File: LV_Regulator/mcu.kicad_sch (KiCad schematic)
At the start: 58 parts, among them J5 SWD, J6 2169890001, U10 25CSM04xxSN, U4 STM32F103C8Tx, Y1 32.768kHz, Y2 8MHz

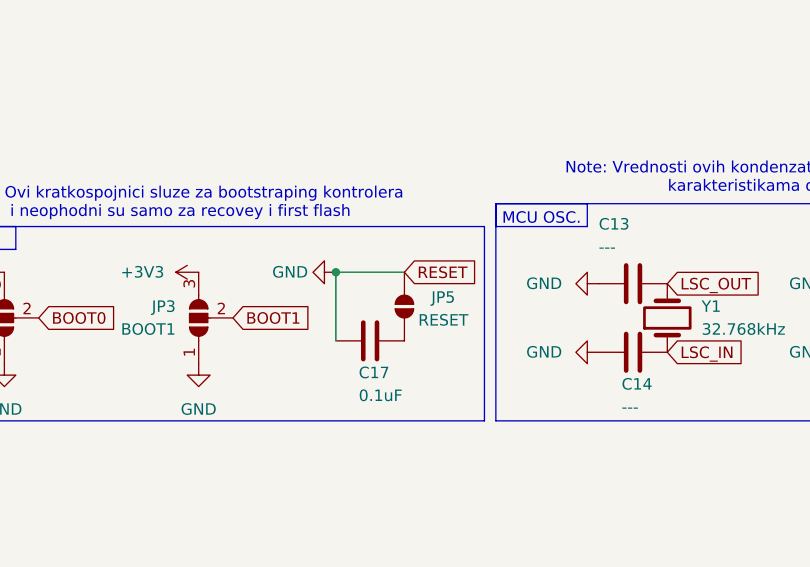
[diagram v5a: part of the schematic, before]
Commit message: Multiple Updates
Added footprints and purchase links to the MCU page and updated some footprints on the Regulator Page from smd to SMD Handsolder
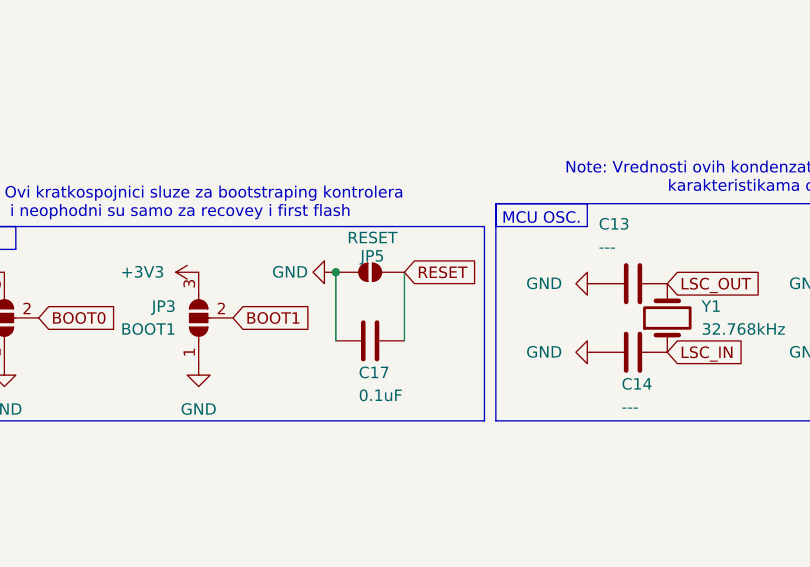
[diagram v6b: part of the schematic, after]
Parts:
- C13, C14, C15, C16: footprint Capacitor_SMD:C_1206_3216Metric -> Capacitor_SMD:C_1206_3216Metric_Pad1.33x1.80mm_HandSolder
- C17, C18, C19, C20, C22, C23: footprint Capacitor_SMD:C_1206_3216Metric -> Capacitor_SMD:C_1206_3216Metric_Pad1.33x1.80mm_HandSolder; Purchase Place (none) -> https://eu.mouser.com/ProductDetail/Murata-Electronics/GRM0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
- C21: footprint Capacitor_SMD:C_1206_3216Metric -> Capacitor_SMD:C_1206_3216Metric_Pad1.33x1.80mm_HandSolder; Purchase Place (none) -> Purchase Placehttps://eu.mouser.com/ProductDetail/Murata-El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
- C34, C35: footprint (none) -> Capacitor_SMD:C_1206_3216Metric_Pad1.33x1.80mm_HandSolder; Purchase Place (none) -> https://eu.mouser.com/ProductDetail/Murata-Electronics/GRM0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
- JP1, JP2, JP3, JP4, JP6, JP7, JP8: footprint Jumper:SolderJumper-3_P1.3mm_Open_Pad1.0x1.5mm -> Jumper:SolderJumper-3_P1.3mm_Open_RoundedPad1.0x1.5mm
- JP5: footprint Jumper:SolderJumper-2_P1.3mm_Open_Pad1.0x1.5mm -> Jumper:SolderJumper-2_P1.3mm_Open_RoundedPad1.0x1.5mm
- JP9: footprint (none) -> Jumper:SolderJumper-3_P1.3mm_Open_RoundedPad1.0x1.5mm
- LED1, LED5, LED8: footprint (none) -> LED_SMD:LED_1206_3216Metric_Pad1.42x1.75mm_HandSolder; Purchase Place (none) -> https://eu.mouser.com/ProductDetail/Kingbright/APL3015MGC?q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
- LED10, LED12, LED7: footprint (none) -> LED_SMD:LED_1206_3216Metric_Pad1.42x1.75mm_HandSolder; Purchase Place (none) -> https://eu.mouser.com/ProductDetail/VCC/CMD11-21VYC-TR8?qs=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
- LED11, LED6, LED9: footprint (none) -> LED_SMD:LED_1206_3216Metric_Pad1.42x1.75mm_HandSolder; Purchase Place (none) -> https://eu.mouser.com/ProductDetail/Kingbright/APT3216LSECK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
- LED2, LED3, LED4: footprint (none) -> LED_SMD:LED_1206_3216Metric_Pad1.42x1.75mm_HandSolder; Purchase Place (none) -> https://eu.mouser.com/ProductDetail/American-Bright-LED/BL-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
- R118, R119: Purchase Place (none) -> https://eu.mouser.com/ProductDetail/Panasonic/ERA-8AHD270V?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
- R120: Purchase Place (none) -> https://eu.mouser.com/ProductDetail/Panasonic/ERA-8ARB152V?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
- R121, R122: Purchase Place (none) -> https://eu.mouser.com/ProductDetail/Panasonic/ERA-8ARB512V?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
- R17, R18, R19, R20, R21, R22, R24, R25, R28: footprint (none) -> Resistor_SMD:R_1206_3216Metric_Pad1.30x1.75mm_HandSolder; Purchase Place (none) -> https://eu.mouser.com/ProductDetail/Panasonic/ERA-8AEB131V?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
- R23, R26, R27: footprint (none) -> Resistor_SMD:R_1206_3216Metric_Pad1.30x1.75mm_HandSolder; Purchase Place (none) -> https://eu.mouser.com/ProductDetail/Panasonic/ERA-8AEB271V?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
- R30: Purchase place (none) -> https://eu.mouser.com/ProductDetail/Panasonic/ERA-8AEB103V?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
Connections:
- net GND: no longer U4.7 (NRST)
- net RESET: now reaches C17.1, JP5.2 (B)
- net RESET: now also U4.7 (NRST)
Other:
- moved on the sheet: JP5

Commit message: Added Footprints & Links for Component Purchase
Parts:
- R30: footprint (none) -> Resistor_SMD:R_1206_3216Metric_Pad1.30x1.75mm_HandSolder
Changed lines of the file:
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@@
 			)
 		)
-		(property "Footprint" ""
+		(property "Footprint" "Resistor_SMD:R_1206_3216Metric_Pad1.30x1.75mm_HandSolder"
 			(at 135.89 94.742 90)
 			(effects

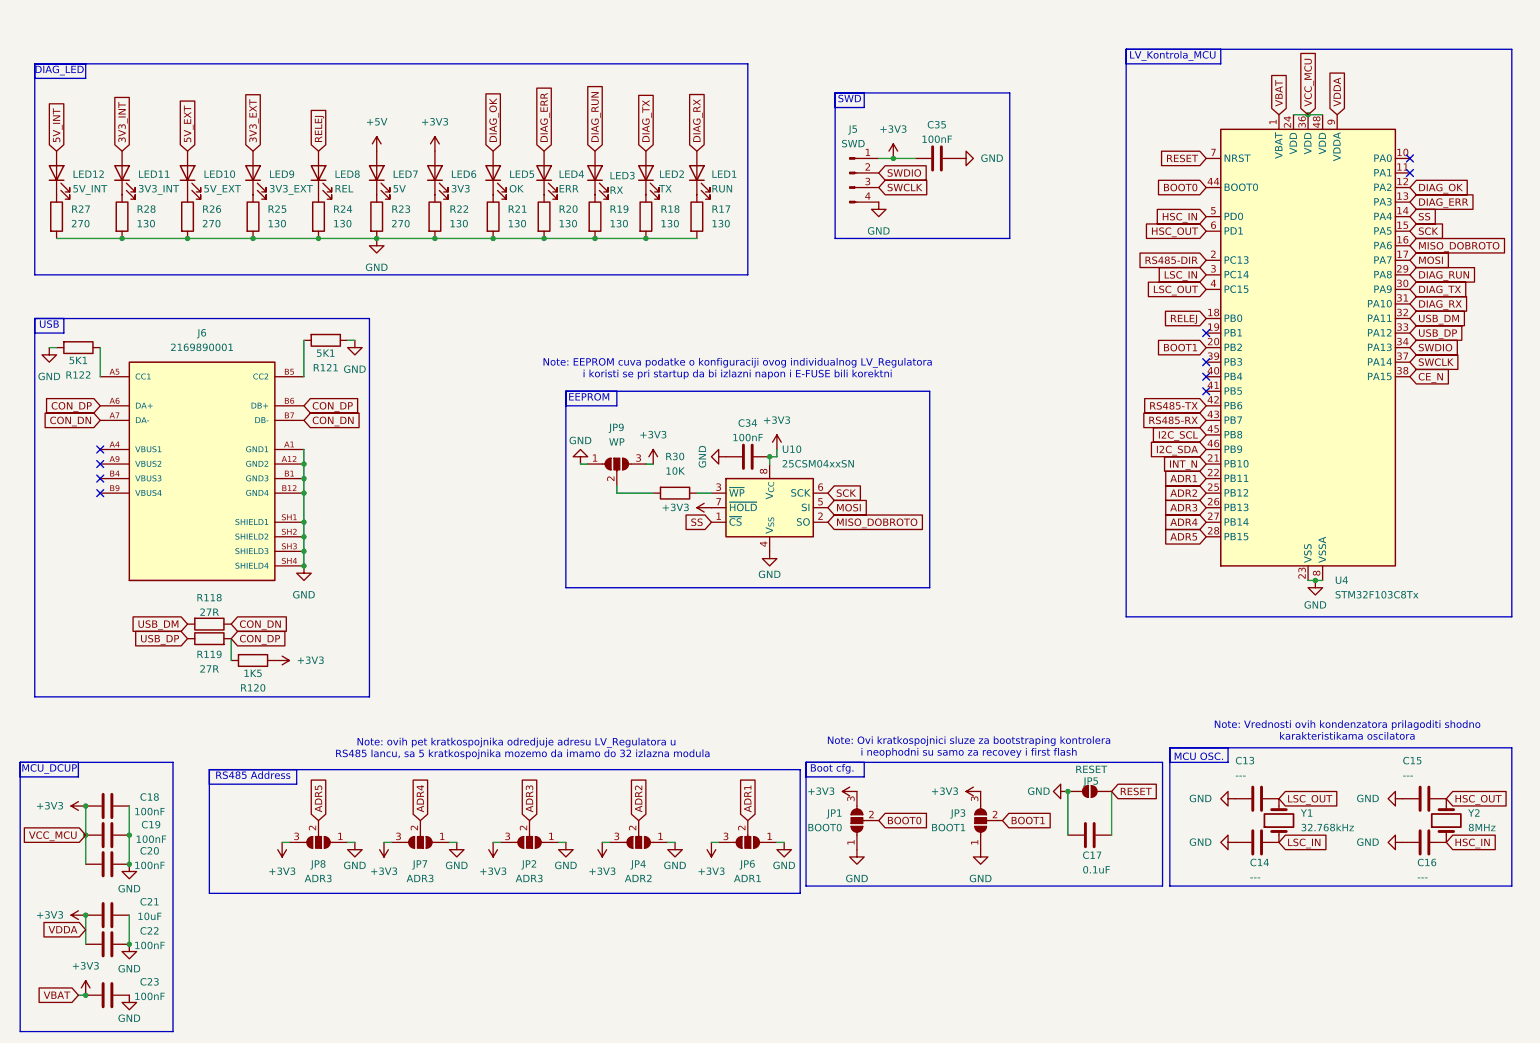
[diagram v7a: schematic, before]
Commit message: Halfway Push of adding 3D models to PCB layout components
Pushing with components left to add to finish on main PC
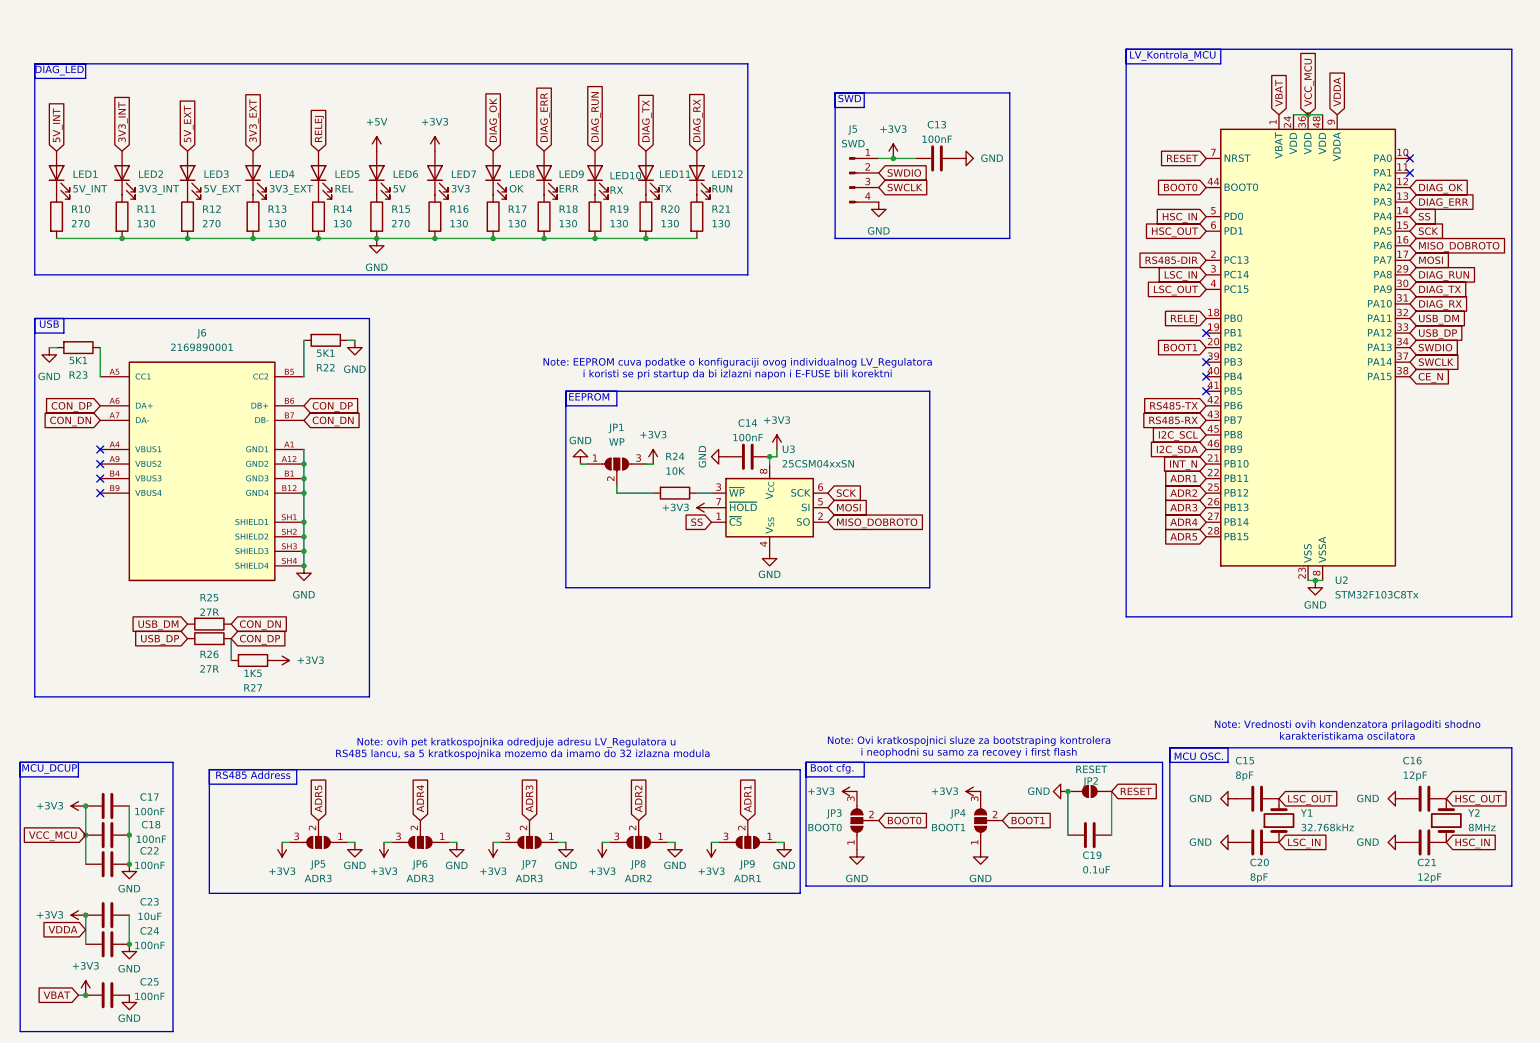
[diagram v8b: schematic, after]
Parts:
- C15: renamed from C13; value --- -> 8pF; Purchase Place (none) -> https://eu.mouser.com/ProductDetail/Walsin/1206N8R0B500CT?q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
- C16: renamed from C15; value --- -> 12pF; Purchase Place (none) -> https://eu.mouser.com/ProductDetail/KYOCERA-AVX/12065A120KA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
- C20: renamed from C14; value --- -> 8pF; Purchase Place (none) -> https://eu.mouser.com/ProductDetail/Walsin/1206N8R0B500CT?q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
- C21: renamed from C16; value --- -> 12pF; Purchase Place (none) -> https://eu.mouser.com/ProductDetail/KYOCERA-AVX/12065A120KA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
- J5: footprint Connector_PinHeader_1.00mm:PinHeader_1x04_P1.00mm_Vertical -> Connector_PinHeader_2.54mm:PinHeader_1x04_P2.54mm_Vertical
- Y1: footprint (none) -> Crystal:Crystal_SMD_EuroQuartz_EQ161-2Pin_3.2x1.5mm_HandSoldering; Purchase Place (none) -> https://eu.mouser.com/ProductDetail/Seiko-Instruments/SC32A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
- Y2: footprint (none) -> Crystal:Crystal_SMD_5032-2Pin_5.0x3.2mm_HandSoldering; Purchase Place (none) -> https://eu.mouser.com/ProductDetail/ECS/ECS-80-8-30-JGN-TR?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
- renumbered C35 to C13, C34 to C14, C18 to C17, C19 to C18, C17 to C19, C20 to C22, C21 to C23, C22 to C24, C23 to C25, JP9 to JP1, JP5 to JP2, JP1 to JP3, JP3 to JP4, JP8 to JP5, JP7 to JP6, JP2 to JP7, JP4 to JP8, JP6 to JP9, LED12 to LED1, LED3 to LED10, LED2 to LED11, LED1 to LED12, LED11 to LED2, LED10 to LED3, LED9 to LED4, LED8 to LED5, LED7 to LED6, LED6 to LED7, LED5 to LED8, LED4 to LED9, R27 to R10, R28 to R11, R26 to R12, R25 to R13, R24 to R14, R23 to R15, R22 to R16, R21 to R17, R20 to R18, R18 to R20, R17 to R21, R121 to R22, R122 to R23, R30 to R24, R118 to R25, R119 to R26, R120 to R27, U4 to U2, U10 to U3
